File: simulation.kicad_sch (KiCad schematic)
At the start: 5 parts

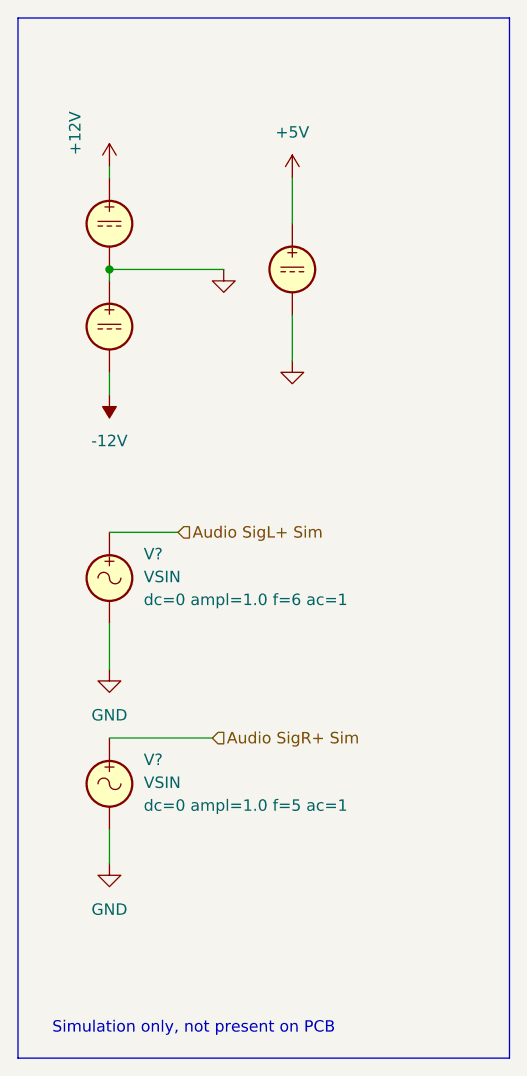
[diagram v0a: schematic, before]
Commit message: Update to KiCad 9
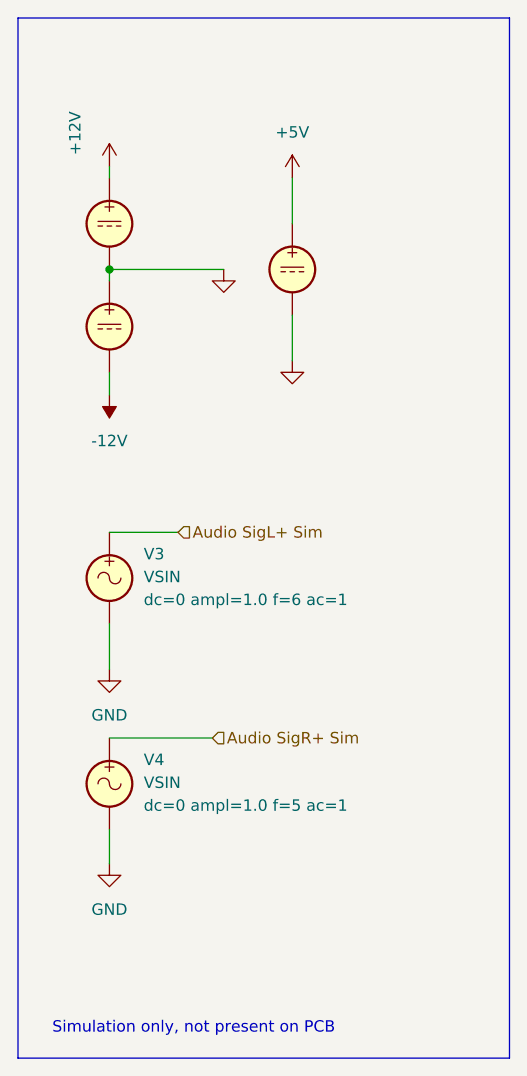
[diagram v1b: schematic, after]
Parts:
- gave numbers to parts that had none: 5
